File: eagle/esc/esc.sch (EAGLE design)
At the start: 9 parts, among them IC1 DRV8305NPHPR, IC2 STM32L431CCT6LQFP48, J1 STLINK-PROG-CON, T1 CSD17573Q5B, T2 CSD17573Q5B, T3 CSD17573Q5B, T4 CSD17573Q5B, T5 CSD17573Q5B, T6 CSD17573Q5B

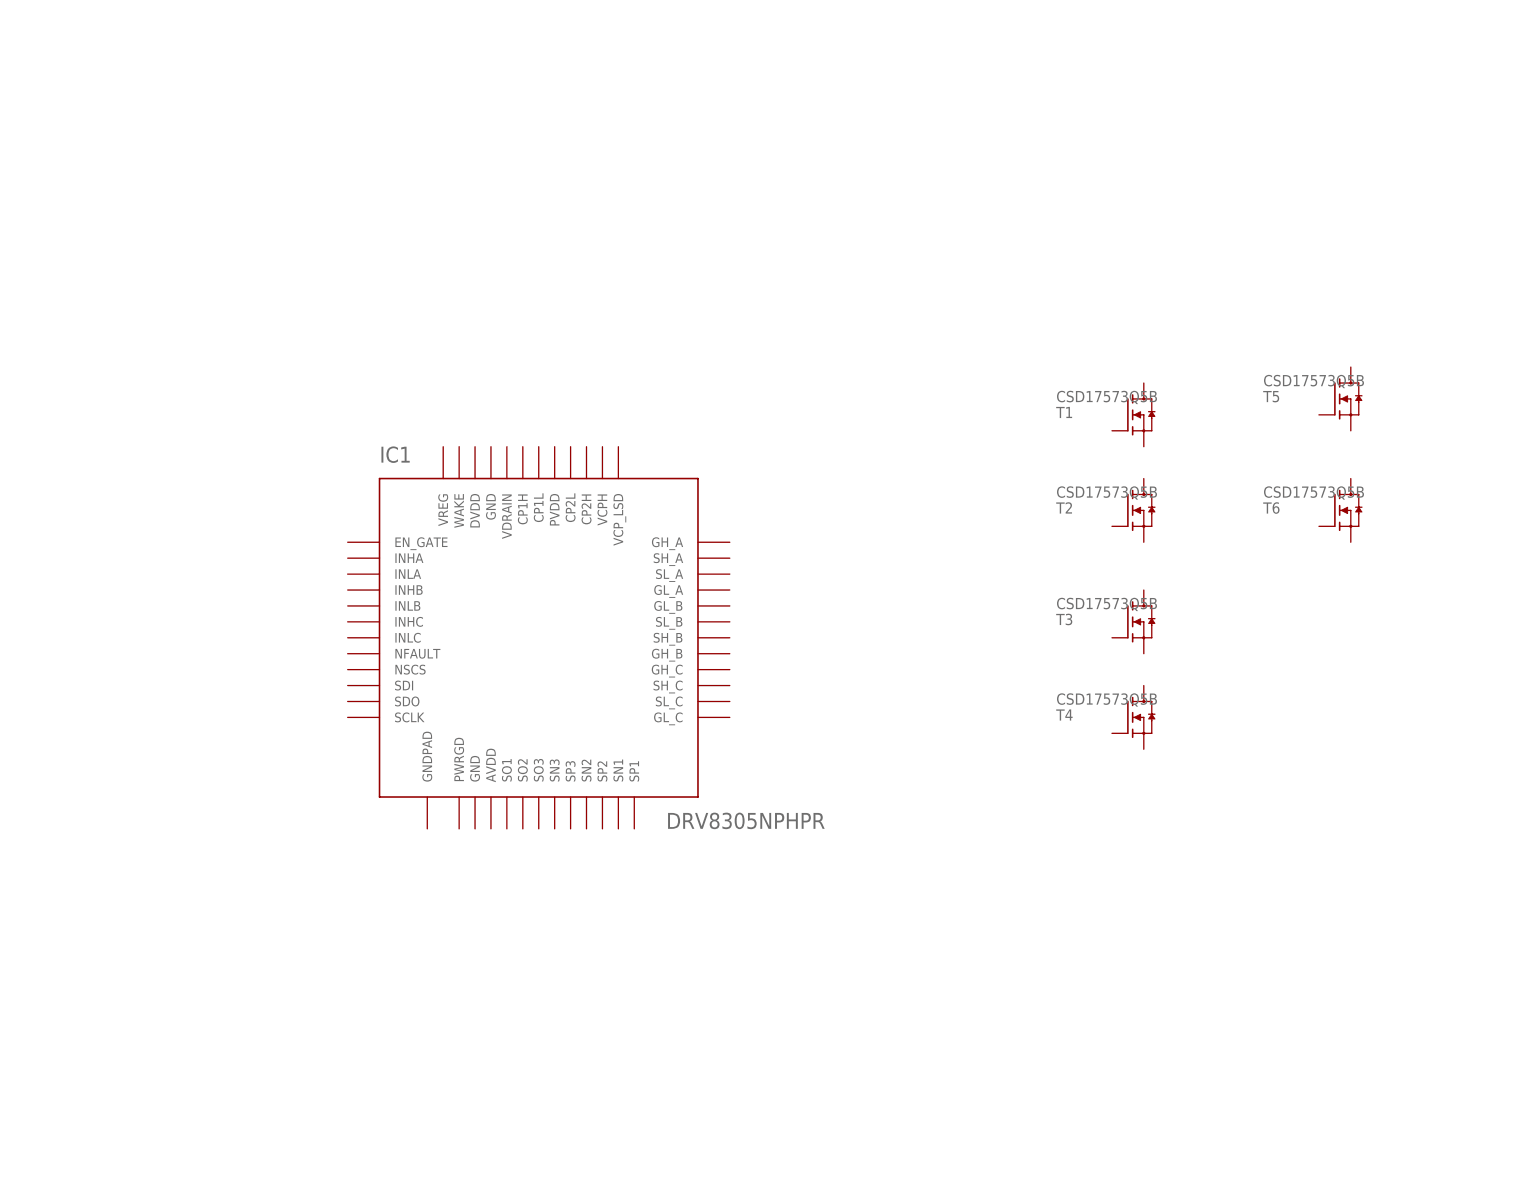
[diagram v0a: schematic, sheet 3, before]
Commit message: added FETs and related circuitry for the motor drive, current sense
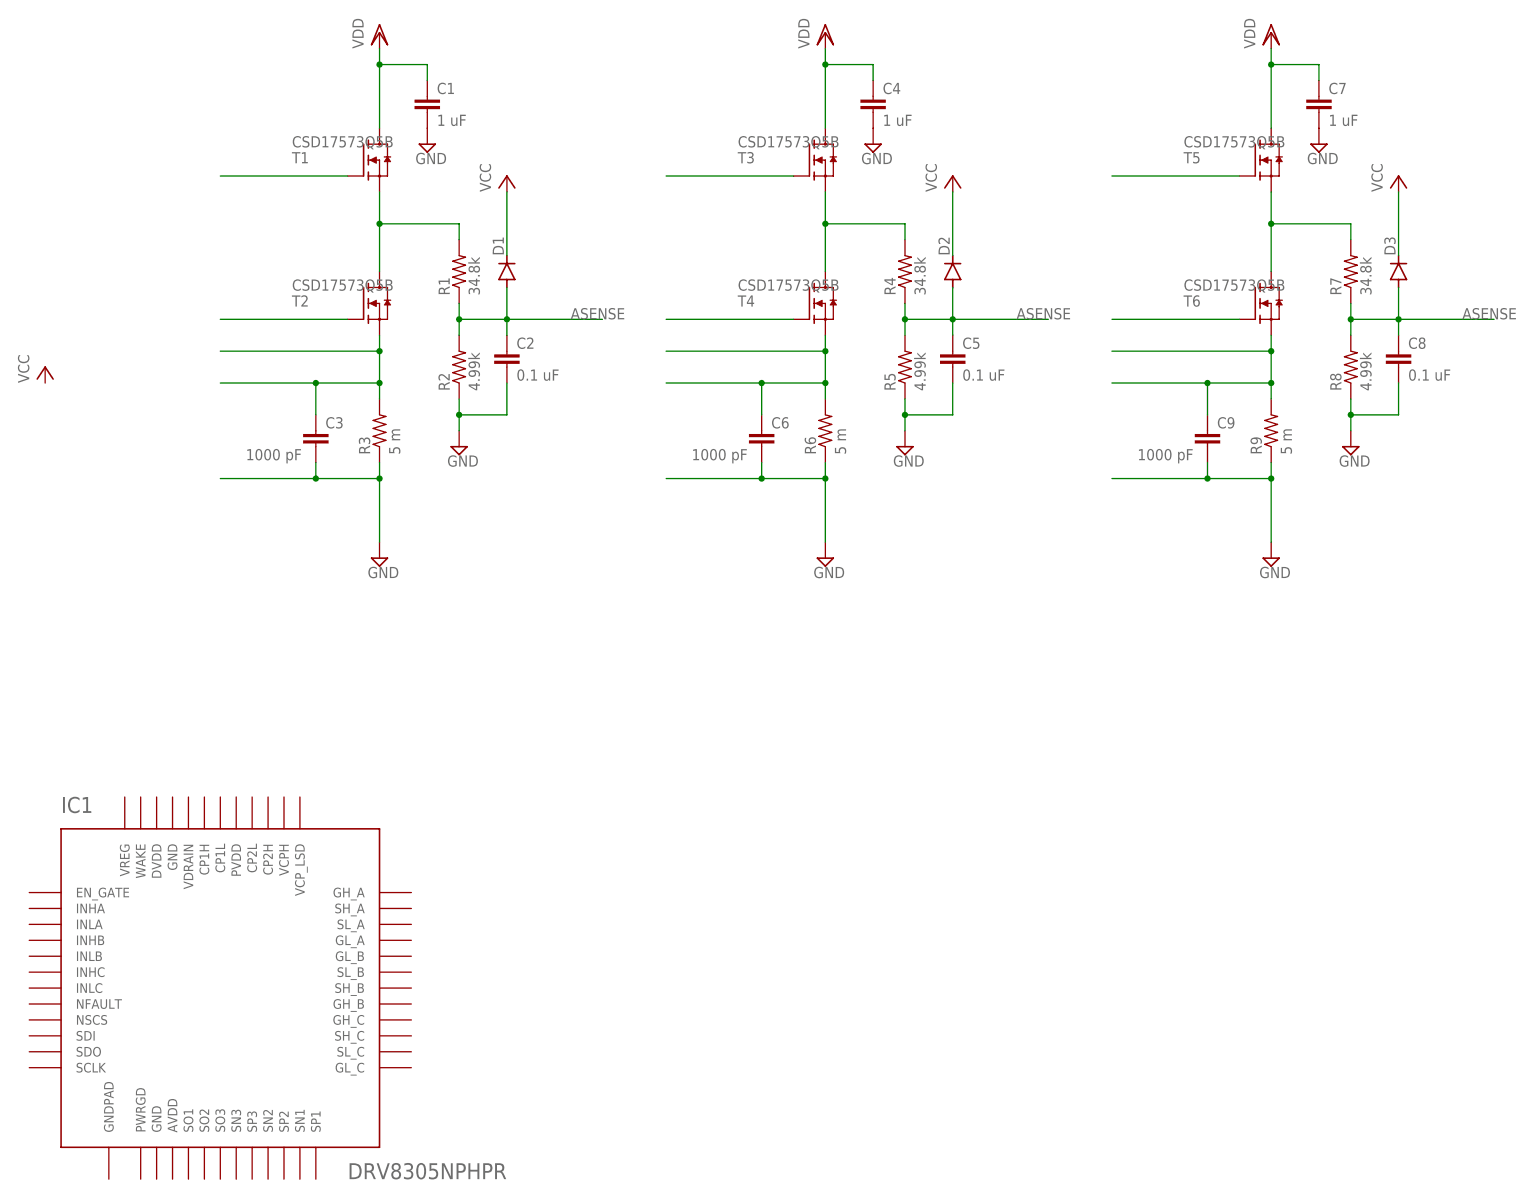
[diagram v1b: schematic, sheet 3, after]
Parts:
- added C1, C4, C7: 1 uF, resistor:C-EUC0603
- added C2, C5, C8: 0.1 uF, resistor:C-EUC0603
- added C3, C6, C9: 1000 pF, resistor:C-EUC0603
- added D1, D2, D3: (no value), diode:DIODE-GF1
- added R1, R4, R7: 34.8k, resistor:R-US_R0603
- added R2, R5, R8: 4.99k, resistor:R-US_R0603
- added R3, R6, R9: 5 m, resistor:R-US_R0603
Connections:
- new net ASENSE: C2.1, C5.1, C8.1, D1.A, D2.A, D3.A, R1.1, R2.2, R4.1, R5.2, R7.1, R8.2
- new net GND: C1.2, C2.2, C3.2, C4.2, C5.2, C6.2, C7.2, C8.2, C9.2, R2.1, R3.1, R5.1, R6.1, R8.1, R9.1
- new net N$1: R1.2, T1.S, T2.D
- new net N$10: C9.1, R9.2, T6.S
- new net N$11: T5.G
- new net N$12: T6.G
- new net N$2: C3.1, R3.2, T2.S
- new net N$3: T1.G
- new net N$4: T2.G
- new net N$5: R4.2, T3.S, T4.D
- new net N$6: C6.1, R6.2, T4.S
- new net N$7: T3.G
- new net N$8: T4.G
- new net N$9: R7.2, T5.S, T6.D
- new net VCC: D1.C, D2.C, D3.C
- new net VDD: C1.1, C4.1, C7.1, T1.D, T3.D, T5.D
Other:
- moved on the sheet: IC1, T1, T2, T3, T4, T5, T6

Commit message: Added most of the components to the schematic. Left to add connectors for SPI port for micro and power connectors
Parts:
- removed J1: STLINK-PROG-CON, qc_esc:STLINK-PROG-CON
- added C10: 470 uF, rcl:CPOL-USE5-10.5
- added C11: 470 uF, rcl:CPOL-USE5-13
- added C12: 4.7 uF, resistor:C-EUC0805
- added C13, C17, C18, C19, C25, C28, C30, C32, C34: 1 uF, resistor:C-EUC0603
- added C14, C16: 0.047 uF, resistor:C-EUC0603
- added C15, C27: 2.2 uF, resistor:C-EUC0603
- added C20, C22, C26, C36: 0.1 uF, resistor:C-EUC0603
- added C21: 0.01 uF, resistor:C-EUC0603
- added C23: 10 uF, qc_esc:CAPACITOR4.3X4.3
- added C24: CAPACITOR4.3X4.3, qc_esc:CAPACITOR4.3X4.3
- added C29, C31, C33, C35: 100 nF, resistor:C-EUC0603
- added D4, D5: STPS2L30ASMA, qc_esc:STPS2L30ASMA
- added J2: ARM10-CON, qc_esc:ARM10-CON
- added LED1, LED2, LED3, LED4: (no value), eagle-ltspice:LED_ESML0603
- added R10: 100, resistor:R-US_R0603
- added R11, R12: 10 k, resistor:R-US_R0603
- added R13: 34.8k, resistor:R-US_R0603
- added R14: 4.99k, resistor:R-US_R0603
- added R15, R16, R17, R18: 10k, resistor:R-US_R0603
- added R19: DNP, resistor:R-US_R0603
- added R20, R21, R22, R23: 1k, resistor:R-US_R0603
- added S1: (no value), switch-omron:10-XX
- added U1: LD1117S50TR1, qc_esc:LD1117S50TR1
- added U2: MIC5319-3.3YD5-TR, qc_esc:MIC5319-3.3YD5-TR
- D1, D2, D3: value (none) -> STPS2L30ASMA; device diode:DIODE-GF1 -> qc_esc:STPS2L30ASMA
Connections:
- new net +5V: C24.+, D5.A, U1.VOUT@1, U1.VOUT@2
- new net BSENSE: C5.1, D2.A, R4.1, R5.2
- new net CSENSE: C8.1, D3.A, R7.1, R8.2
- new net EN_GATE: IC1.EN_GATE
- new net GH_A: IC1.GH_A, T1.G
- new net GH_B: IC1.GH_B, T3.G
- new net GH_C: IC1.GH_C, T5.G
- new net GL_A: IC1.GL_A, T2.G
- new net GL_B: IC1.GL_B, T4.G
- new net GL_C: IC1.GL_C, T6.G
- new net INHA: IC1.INHA
- new net INHB: IC1.INHB
- new net INHC: IC1.INHC
- new net INLA: IC1.INLA
- new net INLB: IC1.INLB
- new net INLC: IC1.INLC
- new net N$13: IC2.PH3/BOOT0, R19.2
- new net N$14: LED1.A, R20.2
- new net N$16: LED2.A, R21.2
- new net N$17: LED3.A, R22.2
- new net N$18: LED4.A, R23.2
- new net NFAULT: IC1.NFAULT, R12.1
- new net NRST: C36.1, IC2.NRST, J2.NRST, S1.P, S1.P1
- new net NSCS: IC1.NSCS
- new net PVDDSENSE: C22.1, D4.A, R13.1, R14.2
- new net PWRGD: IC1.PWRGD, R11.1
- new net SCLK: IC1.SCLK
- new net SDI: IC1.SDI
- new net SDO: IC1.SDO
- new net SH_A: IC1.SH_A, R1.2, T1.S, T2.D
- new net SH_B: IC1.SH_B, R4.2, T3.S, T4.D
- new net SH_C: IC1.SH_C, R7.2, T5.S, T6.D
- new net SL_A: C3.1, IC1.SL_A, R3.2, T2.S
- new net SL_B: C6.1, IC1.SL_B, R6.2, T4.S
- new net SL_C: C9.1, IC1.SL_C, R9.2, T6.S
- new net SN1: IC1.SN1
- new net SN2: IC1.SN2
- new net SN3: IC1.SN3
- new net SO1: IC1.SO1
- new net SO2: IC1.SO2
- new net SO3: IC1.SO3
- new net SP1: IC1.SP1
- new net SP2: IC1.SP2
- new net SP3: IC1.SP3
- new net STS1: LED2.C
- new net STS2: LED3.C
- new net STS3: LED4.C
- new net TCK: J2.TCK, R16.1
- new net TDI: J2.TDI, R18.1
- new net TDO: J2.TDO, R17.1
- new net TMS: J2.TMS, R15.1
- net ASENSE: no longer C5.1, C8.1, D2.A, D3.A, R4.1, R5.2, R7.1, R8.2
- net GND: now also C10.-, C11.-, C12.2, C13.2, C17.2, C18.1, C19.1, C20.1, C21.1, C22.2, C23.-, C24.-, C25.2, C26.2, C27.2, C28.2, C29.2, C30.2, C31.2, C32.2, C33.2, C34.2, C35.2, C36.2, IC1.GND@1, IC1.GND@2, IC1.GNDPAD, IC2.VSS@1, IC2.VSS@2, IC2.VSS@3, IC2.VSSA/VREF-, J2.GDET, J2.GND@1, J2.GND@2, LED1.C, R14.1, R19.1, S1.S, S1.S1, U1.GND, U2.GND
- net N$1: now also C13.1, IC1.VCP_LSD; no longer R1.2, T1.S, T2.D
- net N$10: now also C19.2, IC1.AVDD; no longer C9.1, R9.2, T6.S
- net N$11: now also C25.1, D5.C, U2.EN, U2.VIN; no longer T5.G
- net N$12: now also C26.1, U2.BYP; no longer T6.G
- net N$2: now also C16.1, IC1.CP1L; no longer C3.1, R3.2, T2.S
- net N$3: now also C14.2, IC1.CP2H; no longer T1.G
- net N$4: now also C14.1, IC1.CP2L; no longer T2.G
- net N$5: now also C15.1, IC1.VCPH; no longer R4.2, T3.S, T4.D
- net N$6: now also C16.2, IC1.CP1H; no longer C6.1, R6.2, T4.S
- net N$7: now also C18.2, IC1.VREG; no longer T3.G
- net N$8: now also IC1.VDRAIN, R10.1; no longer T4.G
- net N$9: now also C17.1, IC1.DVDD; no longer R7.2, T5.S, T6.D
- net VCC: now also C27.1, C28.1, C29.1, C30.1, C31.1, C32.1, C33.1, C34.1, C35.1, D4.C, IC2.VBAT, IC2.VDD@1, IC2.VDD@2, IC2.VDD@3, IC2.VDDA/VREF+, J2.VCC, R11.2, R12.2, R15.2, R16.2, R17.2, R18.2, R20.1, R21.1, R22.1, R23.1, U2.VOUT
- net VDD: now also C10.+, C11.+, C12.1, C15.2, C20.2, C21.2, C23.+, IC1.PVDD, R10.2, R13.2, U1.VIN
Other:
- note added: "TODO: connector choices for SPI port, 12V, GND"

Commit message: completed schematic of esc
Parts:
- added C37, C38: 0.1 uF, resistor:C-EUC0603
- added C39: 10 uF, resistor:CPOL-USCT3216
- added IC3: FT232RL, ftdichip:FT232RL
- added R24, R25: (no value), resistor:R-US_R0603
- added X1: C-GRID-02-15-19, con-molex:C-GRID-02-15-19
- added X2: MINI-USB-32005-301, con-cypressindustries:MINI-USB-32005-301
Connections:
- removed net SN1: IC1.SN1
- removed net SN2: IC1.SN2
- removed net SN3: IC1.SN3
- removed net SP1: IC1.SP1
- removed net SP2: IC1.SP2
- removed net SP3: IC1.SP3
- new net I2C_SCL: IC2.PB8, R24.1, X1-1.S
- new net I2C_SDA: IC2.PB9, R25.1, X1-2.S
- new net N$15: C37.1, C39.+, IC3.VCC, X2.1
- new net N$19: C38.1, IC3.3V3OUT, IC3.VCCIO
- new net N$20: IC3.USBDM, X2.2
- new net N$21: IC3.USBDP, X2.3
- new net NJTRST: IC2.PB4, J2.NRST
- new net UART_RX: IC2.PB7, IC3.RXD
- new net UART_TX: IC2.PB6, IC3.TXD
- net ASENSE: now also IC2.PA7
- net BSENSE: now also IC2.PB0
- net CSENSE: now also IC2.PB1
- net EN_GATE: now also IC2.PB2
- net GND: now also C37.2, C38.2, C39.-, IC1.SP1, IC1.SP2, IC1.SP3, IC3.GND, IC3.GND@1, IC3.GND@2, IC3.GND@A, IC3.TEST, X2.5
- net INHA: now also IC2.PA8
- net INHB: now also IC2.PA9
- net INHC: now also IC2.PA10
- net INLA: now also IC2.PA0
- net INLB: now also IC2.PA1
- net INLC: now also IC2.PA2
- net NFAULT: now also IC2.PB10
- net NRST: no longer J2.NRST
- net NSCS: now also IC2.PB12
- net PVDDSENSE: now also IC2.PA6
- net PWRGD: now also IC2.PB11
- net SCLK: now also IC2.PB13
- net SDI: now also IC2.PB15
- net SDO: now also IC2.PB14
- net SL_A: now also IC1.SN1
- net SL_B: now also IC1.SN2
- net SL_C: now also IC1.SN3
- net SO1: now also IC2.PA3
- net SO2: now also IC2.PA4
- net SO3: now also IC2.PA5
- net STS1: now also IC2.PA11
- net STS2: now also IC2.PA12
- net STS3: now also IC2.PB5
- net TCK: now also IC2.PA14
- net TDI: now also IC2.PA15
- net TDO: now also IC2.PB3
- net TMS: now also IC2.PA13
- net VCC: now also R24.2, R25.2
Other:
- note removed: "TODO: connector choices for SPI port, 12V, GND"
- moved on the sheet: C36, LED1, LED2, LED3, LED4, R20, R21, R22, R23, S1
